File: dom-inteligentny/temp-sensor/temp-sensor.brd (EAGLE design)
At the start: 44.8 x 43.3 mm, 18 parts, among them IC1 REG1117, Q1 16MHz, U1 ATMEGA328, U2 MAX487ESA+TCBX, X1 TERMINAL-BLOCK-3.5MM-3-PIN-LO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

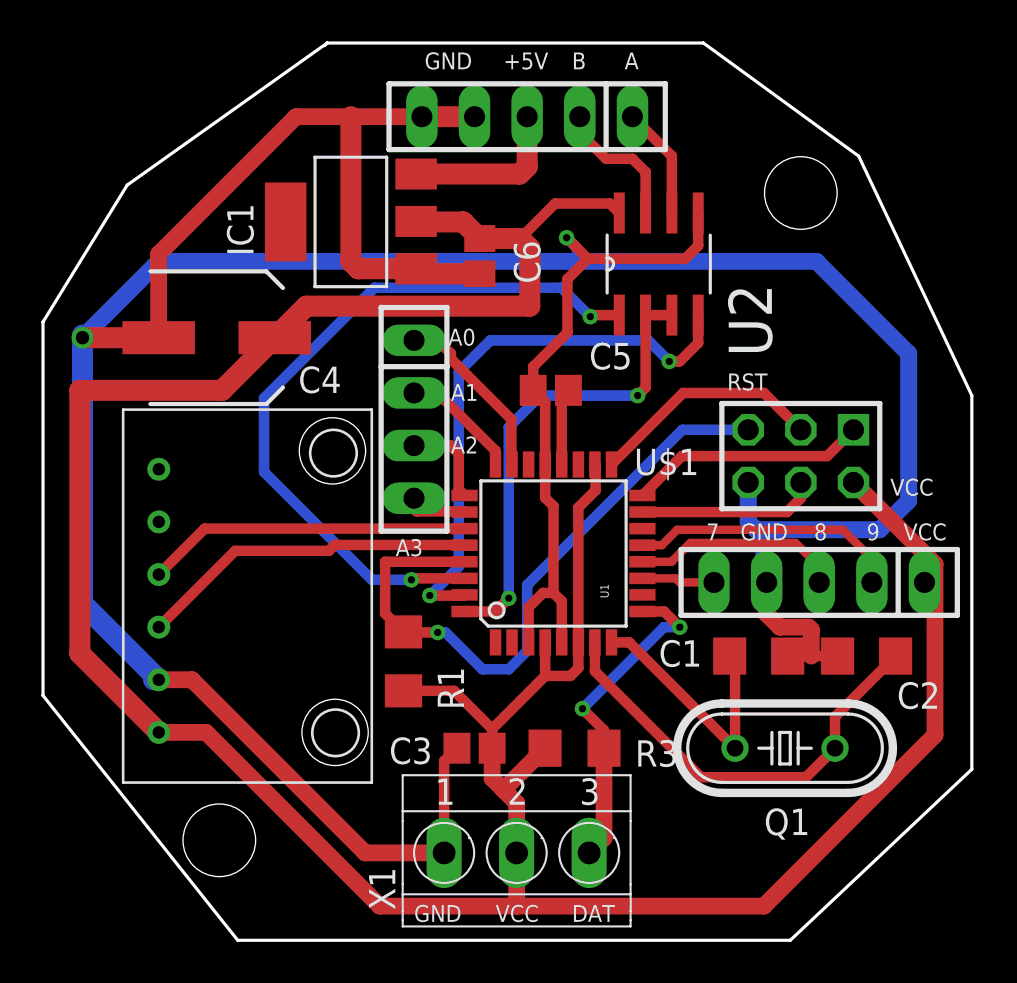
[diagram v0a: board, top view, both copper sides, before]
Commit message: Temp sensor, NTC
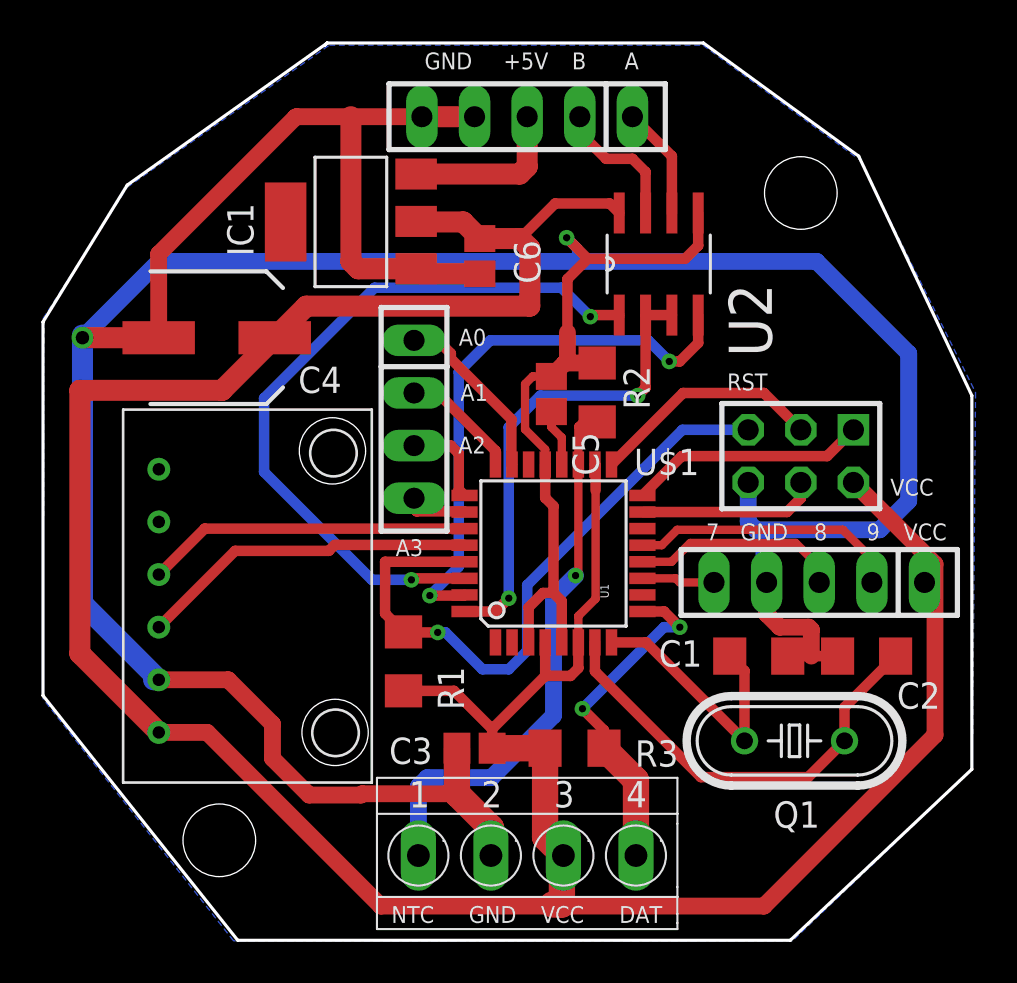
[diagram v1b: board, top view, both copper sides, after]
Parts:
- removed X1: TERMINAL-BLOCK-3.5MM-3-PIN-LONG-PAD, Rembrandt Electronics - Terminal Block 3-5mm v1-0:TERMINAL-BLOCK-3-PIN-3.5MM-LONG-PAD
- added R2: (no value), eagle-ltspice:R1206
- added X2: TERMINAL-BLOCK-3.5MM-4-PIN-LONG-PAD, Rembrandt Electronics - Terminal Block 3-5mm v1-0:TERMINAL-BLOCK-4-PIN-3.5MM-LONG-PAD
- moved Q1 0.58 mm to (39.6, 17.6)
- moved C5 0.18 mm to (27.8, 34.4), turned to 90 degrees
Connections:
- net A6: now also R2.2, X2.1
- net D5: now also X2.4; no longer X1.3
- net GND: now also R2.1, X2.2; no longer X1.1
- net VCC: now also X2.3; no longer X1.2
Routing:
- net A6: track 0.00 -> 26.7 mm, vias 0 -> 1
- net GND: track 184.6 -> 188.0 mm
- net AREF: track 3.72 -> 2.76 mm
- added copper zone on layer 16, net GND
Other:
- board text added: "NTC"
